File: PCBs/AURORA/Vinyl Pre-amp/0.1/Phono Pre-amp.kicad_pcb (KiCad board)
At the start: 2 copper layers, 65 x 55 mm, 59 parts, among them J1 Conn_01x02_Pin, J2 Conn_01x03_Male, J3 Conn_01x03_Male, J4 Conn_01x03_Male, J5 Conn_01x03_Male, J6 Conn_01x03_Pin, U1 OPA2134, U2 OPA2134

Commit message: Updates
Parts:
- moved J1 1.00 mm to (192.1, 98.1)
- moved J2 1.00 mm to (193.3, 108.1)
- moved R17 0.20 mm to (152.0, 133.8)
- moved R18 0.20 mm to (159.0, 133.8)
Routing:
- net V+: track 0.00 -> 123.9 mm
- net V-: track 0.00 -> 93.9 mm
- net LEFTIN: track 0.00 -> 62.2 mm, vias 0 -> 1
- net LEFTOUT: track 0.00 -> 53.7 mm
- net Net-(U2-OutB): track 0.00 -> 48.1 mm, vias 0 -> 1
- net RIGHTIN: track 0.00 -> 38.8 mm, vias 0 -> 1
- net Net-(U1-OutB): track 0.00 -> 37.5 mm
- net Net-(U2-InA-): track 0.00 -> 33.8 mm, vias 0 -> 1
- net Net-(U1-InA-): track 0.00 -> 32.2 mm, vias 0 -> 1
- net RIGHTOUT: track 0.00 -> 29.7 mm
- net Net-(U2-InB-): track 0.00 -> 27.0 mm, vias 0 -> 1
- net Net-(U1-InB-): track 0.00 -> 26.0 mm, vias 0 -> 1
- net Net-(U1-InB+): track 0.00 -> 24.9 mm
- net Net-(U2-InB+): track 0.00 -> 23.9 mm
- net Net-(C5-Pad2): track 0.00 -> 21.5 mm, vias 0 -> 1
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
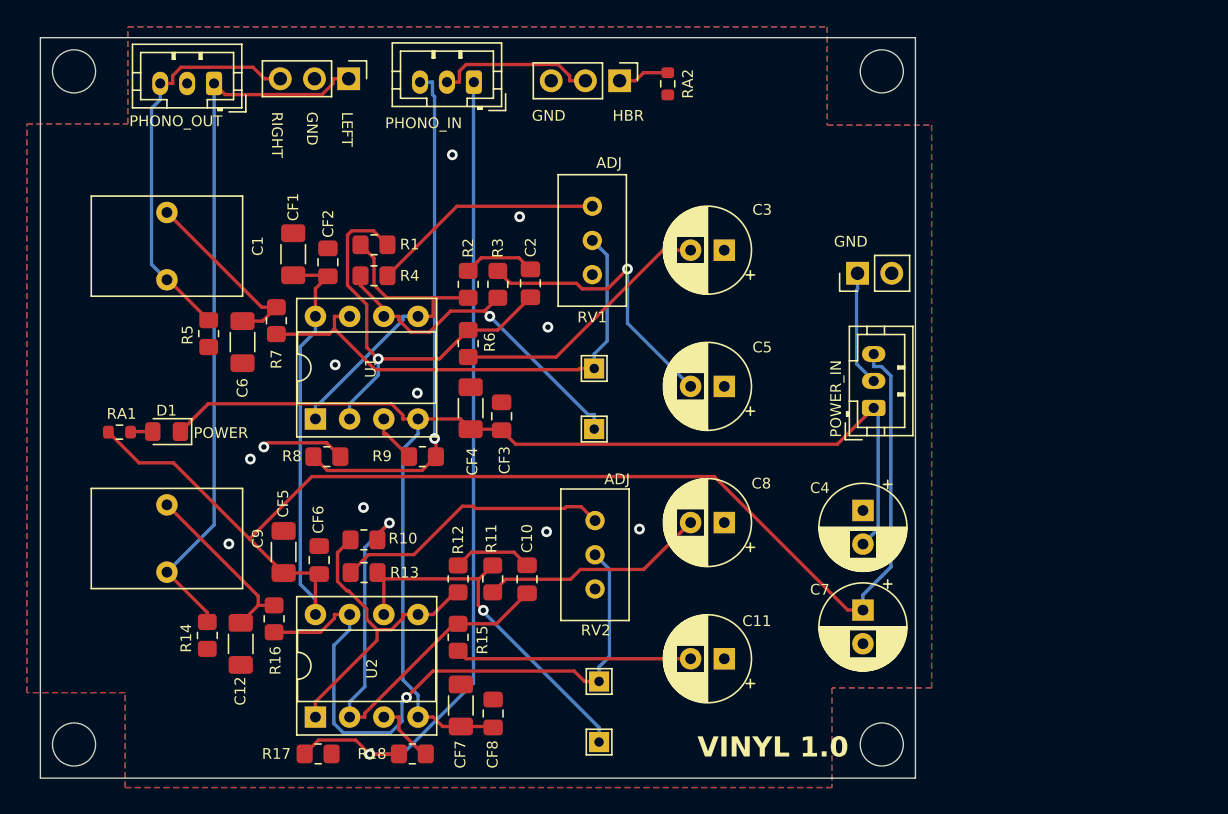
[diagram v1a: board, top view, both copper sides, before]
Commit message: Fixing audio issues, leave TRUNC off and at 24 bits
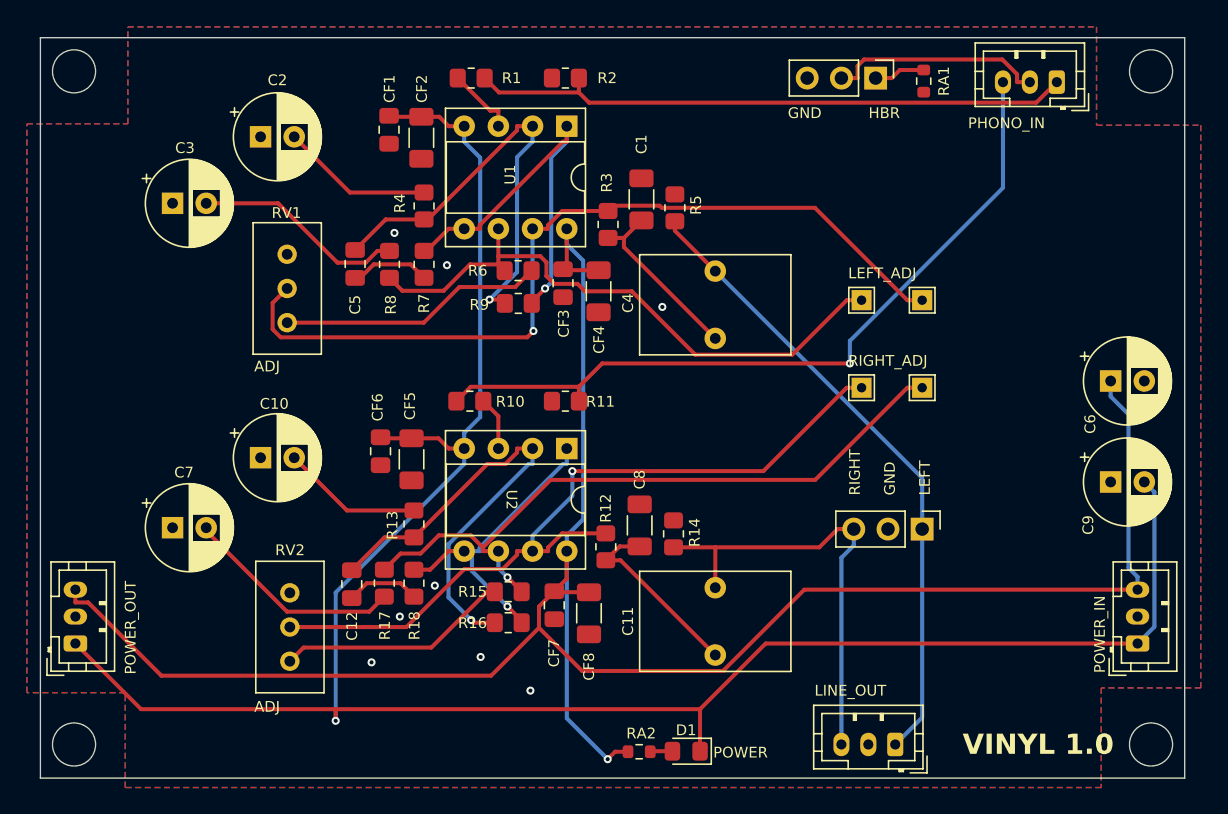
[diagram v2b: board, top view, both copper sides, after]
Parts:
- removed the J1 at (192.1, 98.1)
- added J6: Conn_01x03_Male, Connector_JST:JST_PH_B3B-PH-K_1x03_P2.00mm_Vertical, F.Cu at (134.0, 125.6)
- moved J5 70.5 mm to (194.9, 133.1)
- moved J3 54.2 mm to (196.9, 117.1)
- moved R2 53.5 mm to (170.4, 83.6), turned to 0 degrees
- moved C11 52.3 mm to (181.5, 126.5), turned to 90 degrees
- moved C2 51.9 mm to (147.8, 88.0), turned to 0 degrees
- moved R1 50.4 mm to (163.4, 83.6), turned to 180 degrees
- moved U1 47.7 mm to (170.5, 87.2), turned to -90 degrees
- moved C3 47.4 mm to (141.2, 92.9), turned to 0 degrees
- moved R5 47.1 mm to (178.5, 93.2), turned to -90 degrees
- moved D1 45.3 mm to (179.4, 133.6)
- moved RA2 45.3 mm to (175.9, 133.6)
- moved C1 44.5 mm to (176.0, 92.6), turned to -90 degrees
- moved CF1 44.0 mm to (157.3, 87.4), turned to 90 degrees
- moved J2 43.3 mm to (206.9, 83.9)
- moved C4 42.6 mm to (181.5, 102.9), turned to 90 degrees
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- renumbered C12 to C1, C3 to C10, C1 to C11, C2 to C12, C11 to C2, C8 to C3, C9 to C4, C10 to C5, C7 to C6, C5 to C7, C6 to C8, C4 to C9, CF8 to CF1, CF7 to CF2, CF6 to CF3, CF5 to CF4, CF4 to CF5, CF3 to CF6, CF2 to CF7, CF1 to CF8, J6 to J1, J5 to J2, J2 to J4, J4 to J5, R18 to R1, R9 to R10, R8 to R11, R7 to R12, R6 to R13, R5 to R14, R4 to R15, R1 to R16, R3 to R17, R2 to R18, R17 to R2, R16 to R3, R15 to R4, R14 to R5, R13 to R6, R12 to R7, R11 to R8, R10 to R9, RA2 to RA1, RA1 to RA2, RV2 to RV1, RV1 to RV2, TP4 to TP1, TP3 to TP2, TP1 to TP3, TP2 to TP4, U2 to U1, U1 to U2
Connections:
- J4 pad 2: PGND -> AGND
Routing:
- net V-: track 93.9 -> 161.3 mm, vias 0 -> 1
- net V+: track 123.9 -> 162.1 mm, vias 0 -> 1
- net Net-(U2-InB-): track 26.0 -> 51.5 mm
- net Net-(U2-OutB): track 37.5 -> 57.9 mm, vias 0 -> 1
- net RIGHTIN: track 38.8 -> 57.1 mm
- net Net-(U1-InB-): track 27.0 -> 44.9 mm, vias 1 -> 0
- net LEFTIN: track 62.2 -> 45.0 mm, vias 1 -> 0
- net Net-(U1-OutB): track 48.1 -> 63.6 mm
- net Net-(C10-Pad2): track 19.8 -> 10.5 mm
- net PGND: track 8.56 -> 0.00 mm
- net LEFTOUT: track 53.7 -> 47.3 mm
- net AGND: track 6.23 -> 0.00 mm, vias 11 -> 8
- net Net-(C2-Pad2): track 17.5 -> 11.4 mm
- net Net-(U1-InB+): track 23.9 -> 29.5 mm, vias 0 -> 1
- net Net-(C7-Pad2): track 21.5 -> 16.4 mm, vias 1 -> 0
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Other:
- board size 65 x 55 mm -> 85 x 55 mm
- board text added: "LEFT_ADJ"
- board text added: "LINE_OUT"
- board text added: "POWER_OUT"
- board text added: "RIGHT_ADJ"
- board text removed: "PHONO_OUT"
